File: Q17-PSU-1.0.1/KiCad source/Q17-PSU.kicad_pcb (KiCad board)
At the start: 2 copper layers, 102 x 102 mm, 35 parts, among them J1-1 AC1-1, J1-2 AC1-2, J1-3 AC2-1, J1-4 AC2-2, J2-1 V+, J2-1'1 V+, J2-2 GNDPWR, J2-2'1 GNDPWR, J2-3 V-, J2-4'1 V-

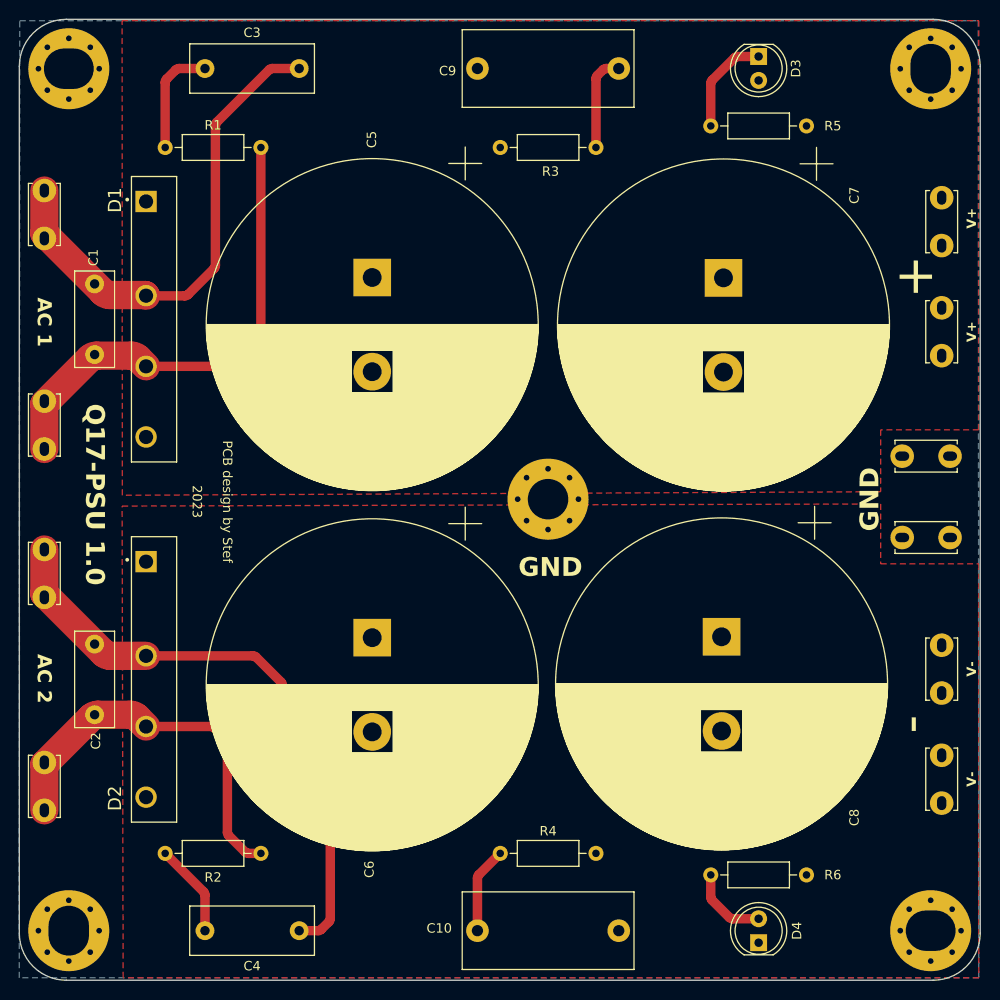
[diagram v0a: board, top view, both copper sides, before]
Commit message: Q17-PSU 1.0.1
Added one Faston connector on GND.
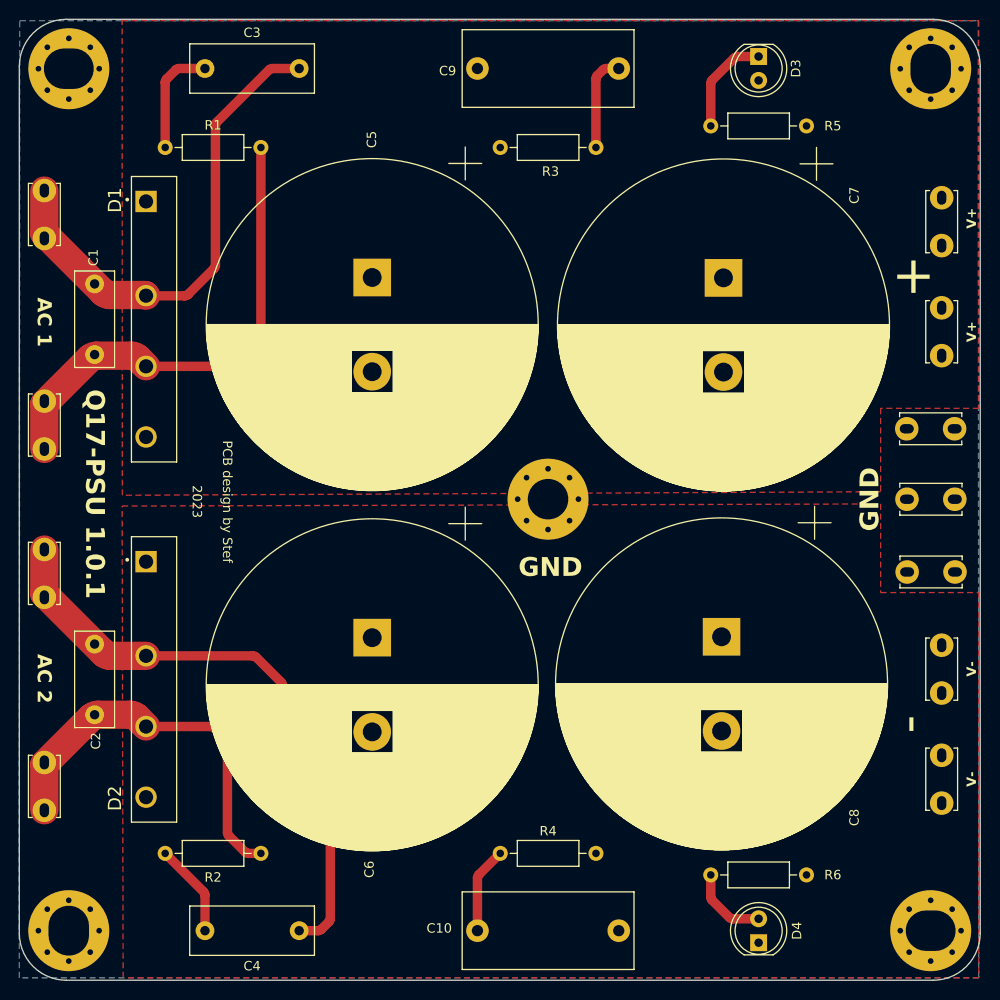
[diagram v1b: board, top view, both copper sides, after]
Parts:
- added J2-4: GNDPWR, Q17_Library:Faston_Connector_63849-1_TEC, F.Cu at (192.3, 90.9)
- moved J2-5 3.70 mm to (192.3, 98.7)
- moved J2-3 2.95 mm to (192.3, 83.5)
- renumbered J2-1'1 to J2-2, J2-2 to J2-3, J2-2'1 to J2-5, J2-3 to J2-6, J2-4'1 to J2-7
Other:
- board text added: "Q17-PSU 1.0.1"
- board text removed: "Q17-PSU 1.0"
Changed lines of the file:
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@@
     (title "Q17 Power Supply")
     (date "2023-08-21")
-    (rev "1.0")
+    (rev "1.0.1")
     (company "by stef")
   )
@@
       (drillshape 0)
       (scaleselection 1)
-      (outputdirectory "/Users/sleclerc/Desktop/Q17/Q17-PSU 1.0/Gerber-Q17-PSU")
+      (outputdirectory "/Users/sleclerc/Desktop/Q17/Q17-PSU 1.0.1/Gerber-Q17-PSU")
     )
   )
@@
   )
   (footprint "Q17_Library:Faston_Connector_63849-1_TEC" (layer "F.Cu")
-    (at 191.77 94.996 180)
+    (at 192.278 90.932 180)
     (property "Mouser" "571-638241")
     (property "Part#" "TE Connectivity 63849-1")
@@
     (property "ki_keywords" "screw terminal")
     (attr through_hole)
-    (fp_text reference "J2-2'1" (at -2.54 2.54) (layer "F.SilkS") hide
+    (fp_text reference "J2-4" (at -2.54 2.54) (layer "F.SilkS") hide
+        (effects (font (size 1 1) (thickness 0.15)))
+    )
+    (fp_text value "GNDPWR" (at -2.286 3.048) (layer "F.SilkS") hide
+        (effects (font (size 1 1) (thickness 0.2) bold))
+    )
+    (fp_line (start -5.842 -1.6891) (end -5.842 -1.28524)
+      (stroke (width 0.12) (type solid)) (layer "F.SilkS"))
+    (fp_line (start -5.842 1.28524) (end -5.842 1.6891)
+      (stroke (width 0.12) (type solid)) (layer "F.SilkS"))
+    (fp_line (start -5.842 1.6891) (end 0.762 1.6891)
+      (stroke (width 0.12) (type solid)) (layer "F.SilkS"))
+    (fp_line (start 0.762 -1.6891) (end -5.842 -1.6891)
+      (stroke (width 0.12) (type solid)) (layer "F.SilkS"))
+    (fp_line (start 0.762 -1.27) (end 0.762 -1.6891)
+      (stroke (width 0.12) (type solid)) (layer "F.SilkS"))
+    (fp_line (start 0.762 1.6891) (end 0.762 1.27)
+      (stroke (width 0.12) (type solid)) (layer "F.SilkS"))
+    (fp_line (start -6.477 -1.8161) (end 1.397 -1.8161)
+      (stroke (width 0.05) (type solid)) (layer "F.CrtYd"))
+    (fp_line (start -6.477 1.8161) (end -6.477 -1.8161)
+      (stroke (width 0.05) (type solid)) (layer "F.CrtYd"))
+    (fp_line (start 1.397 -1.8161) (end 1.397 1.8161)
+      (stroke (width 0.05) (type solid)) (layer "F.CrtYd"))
+    (fp_line (start 1.397 1.8161) (end -6.477 1.8161)
+      (stroke (width 0.05) (type solid)) (layer "F.CrtYd"))
+    (fp_line (start -5.715 -1.5621) (end -5.715 1.5621)
+      (stroke (width 0.1) (type solid)) (layer "F.Fab"))
+    (fp_line (start -5.715 1.5621) (end 0.635 1.5621)
+      (stroke (width 0.1) (type solid)) (layer "F.Fab"))
+    (fp_line (start 0.635 -1.5621) (end -5.715 -1.5621)
+      (stroke (width 0.1) (type solid)) (layer "F.Fab"))
+    (fp_line (start 0.635 1.5621) (end 0.635 -1.5621)
+      (stroke (width 0.1) (type solid)) (layer "F.Fab"))
+    (pad "1" thru_hole circle (at -5.08 0 180) (size 2.5 2.5) (drill oval 1.5 1) (layers "*.Cu" "*.Mask")
+      (net 1 "GNDPWR") (pinfunction "Pin_1") (pintype "passive"))
+    (pad "1" thru_hole circle (at 0 0 180) (size 2.5 2.5) (drill oval 1.5 1) (layers "*.Cu" "*.Mask")
+      (net 1 "GNDPWR") (pinfunction "Pin_1") (pintype "passive"))
+    (model "${KIPRJMOD}/Library/3dmodels/c-63849-1-g-3d.stp"
+      (offset (xyz -2.5 0 9))
+      (scale (xyz 1 1 1))
+      (rotate (xyz -180 -180 0))
+    )
+  )
+  (footprint "Q17_Library:Faston_Connector_63849-1_TEC" (layer "F.Cu")
+    (at 192.295665 98.653992 180)
+    (property "Mouser" "571-638241")
+    (property "Part#" "TE Connectivity 63849-1")
+    (property "Sheetfile" "Q17-PSU.kicad_sch")
+    (property "Sheetname" "")
+    (property "ki_description" "Generic screw terminal, single row, 01x01, script generated (kicad-library-utils/schlib/autogen/connector/)")
+    (property "ki_keywords" "screw terminal")
+    (attr through_hole)
+    (fp_text reference "J2-5" (at -2.54 2.54) (layer "F.SilkS") hide
         (effects (font (size 1 1) (thickness 0.15)))
     )
@@
     (property "ki_keywords" "screw terminal")
     (attr through_hole)
-    (fp_text reference "J2-1'1" (at -2.54 2.54 90) (layer "F.SilkS") hide
+    (fp_text reference "J2-2" (at -2.54 2.54 90) (layer "F.SilkS") hide
         (effects (font (size 1 1) (thickness 0.15)))
     )
@@
   )
   (footprint "Q17_Library:Faston_Connector_63849-1_TEC" (layer "F.Cu")
-    (at 191.77 86.36 180)
+    (at 192.255665 83.453992 180)
     (property "Mouser" "571-638241")
     (property "Part#" "TE Connectivity 63849-1")
@@
     (property "ki_keywords" "screw terminal")
     (attr through_hole)
-    (fp_text reference "J2-2" (at -2.54 2.54) (layer "F.SilkS") hide
+    (fp_text reference "J2-3" (at -2.54 2.54) (layer "F.SilkS") hide
         (effects (font (size 1 1) (thickness 0.15)))
     )
@@
     (property "ki_keywords" "screw terminal")
     (attr through_hole)
-    (fp_text reference "J2-3" (at -2.54 2.54 90) (layer "F.SilkS") hide
+    (fp_text reference "J2-6" (at -2.54 2.54 90) (layer "F.SilkS") hide
         (effects (font (size 1 1) (thickness 0.15)))
     )
@@
     (property "ki_keywords" "screw terminal")
     (attr through_hole)
-    (fp_text reference "J2-4'1" (at -2.54 2.54 90) (layer "F.SilkS") hide
+    (fp_text reference "J2-7" (at -2.54 2.54 90) (layer "F.SilkS") hide
         (effects (font (size 1 1) (thickness 0.15)))
     )
@@
   (gr_line (start 206.629 129.794) (end 78.359 129.794)
     (stroke (width 0.15) (type default)) (layer "Eco1.User"))
-  (gr_rect (start 196.93 96.774) (end 201.93 97.9)
-    (stroke (width 0.025) (type default)) (fill none) (layer "Eco1.User"))
   (gr_line (start 154.178 38.862) (end 154.178 143.51)
     (stroke (width 0.15) (type default)) (layer "Eco1.User"))
-  (gr_rect (start 196.89 83.456) (end 201.89 84.582)
-    (stroke (width 0.025) (type default)) (fill none) (layer "Eco1.User"))
   (gr_rect (start 194.136 112.268) (end 199.136 117.268)
     (stroke (width 0.025) (type default)) (fill none) (layer "Eco1.User"))
@@
   (gr_line (start 211.836 52.07) (end 83.566 52.07)
     (stroke (width 0.15) (type default)) (layer "Eco1.User"))
-  (gr_rect (start 192.358 88.226) (end 197.358 93.226)
-    (stroke (width 0.025) (type default)) (fill none) (layer "Eco1.User"))
   (gr_line (start 114.808 39.116) (end 114.808 143.764)
     (stroke (width 0.15) (type default)) (layer "Eco1.User"))
@@
     (effects (font (size 2 2) (thickness 0.3) bold) (justify bottom))
   )
-  (gr_text "-" (at 191.008 114.808 270) (layer "F.SilkS")
+  (gr_text "-" (at 190.754 114.808 270) (layer "F.SilkS")
     (effects (font (size 4 4) (thickness 0.5)) (justify bottom))
   )
@@
     (effects (font (size 1 1) (thickness 0.15)) (justify bottom))
   )
-  (gr_text "Q17-PSU 1.0" (at 104.902 80.772 270) (layer "F.SilkS")
+  (gr_text "Q17-PSU 1.0.1" (at 104.902 79.248 270) (layer "F.SilkS")
     (effects (font (size 2 2) (thickness 0.4) bold) (justify left bottom))
   )
@@
     (effects (font (size 2 2) (thickness 0.3) bold) (justify bottom))
   )
-  (gr_text "+" (at 191.008 67.31 270) (layer "F.SilkS")
+  (gr_text "+" (at 190.754 67.31 270) (layer "F.SilkS")
     (effects (font (size 4 4) (thickness 0.5)) (justify bottom))
   )
@@
       (pts
         (xy 199.898 40.132)
-        (xy 199.898 83.566)
-        (xy 189.484 83.566)
+        (xy 199.898 81.28)
+        (xy 189.484 81.28)
         (xy 189.484 90.135773)
         (xy 108.986719 90.511645)
@@
       (pts
         (xy 189.483981 91.433055)
-        (xy 189.484 97.79)
-        (xy 199.898 97.79)
+        (xy 189.484 100.838)
+        (xy 199.898 100.838)
         (xy 199.898 141.732)
         (xy 109.0752 141.732)
